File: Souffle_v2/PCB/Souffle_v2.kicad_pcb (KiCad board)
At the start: 2 copper layers, 137.2 x 109.2 mm, 81 parts, among them J1 LED, J2 4PIN, J3 OLED, SW1 SW_PUSH, SW10 SW_PUSH, SW11 SW_PUSH, SW12 SW_PUSH, SW13 SW_PUSH, SW14 SW_PUSH, SW15 SW_PUSH, SW16 SW_PUSH, SW17 SW_PUSH, SW18 SW_PUSH, SW19 SW_PUSH, SW2 SW_PUSH, SW20 SW_PUSH, SW21 SW_PUSH, SW22 SW_PUSH, SW23 SW_PUSH, SW24 SW_PUSH, SW25 SW_PUSH, SW25b1 RotaryEncoder_Switch, SW26 SW_PUSH, SW27 SW_PUSH, SW28 SW_PUSH, SW29 SW_PUSH, SW3 SW_PUSH, SW30 SW_PUSH, SW4 SW_PUSH, SW5 SW_PUSH, SW6 SW_PUSH, SW7 SW_PUSH, SW8 SW_PUSH, SW9 SW_PUSH, U1 ProMicro

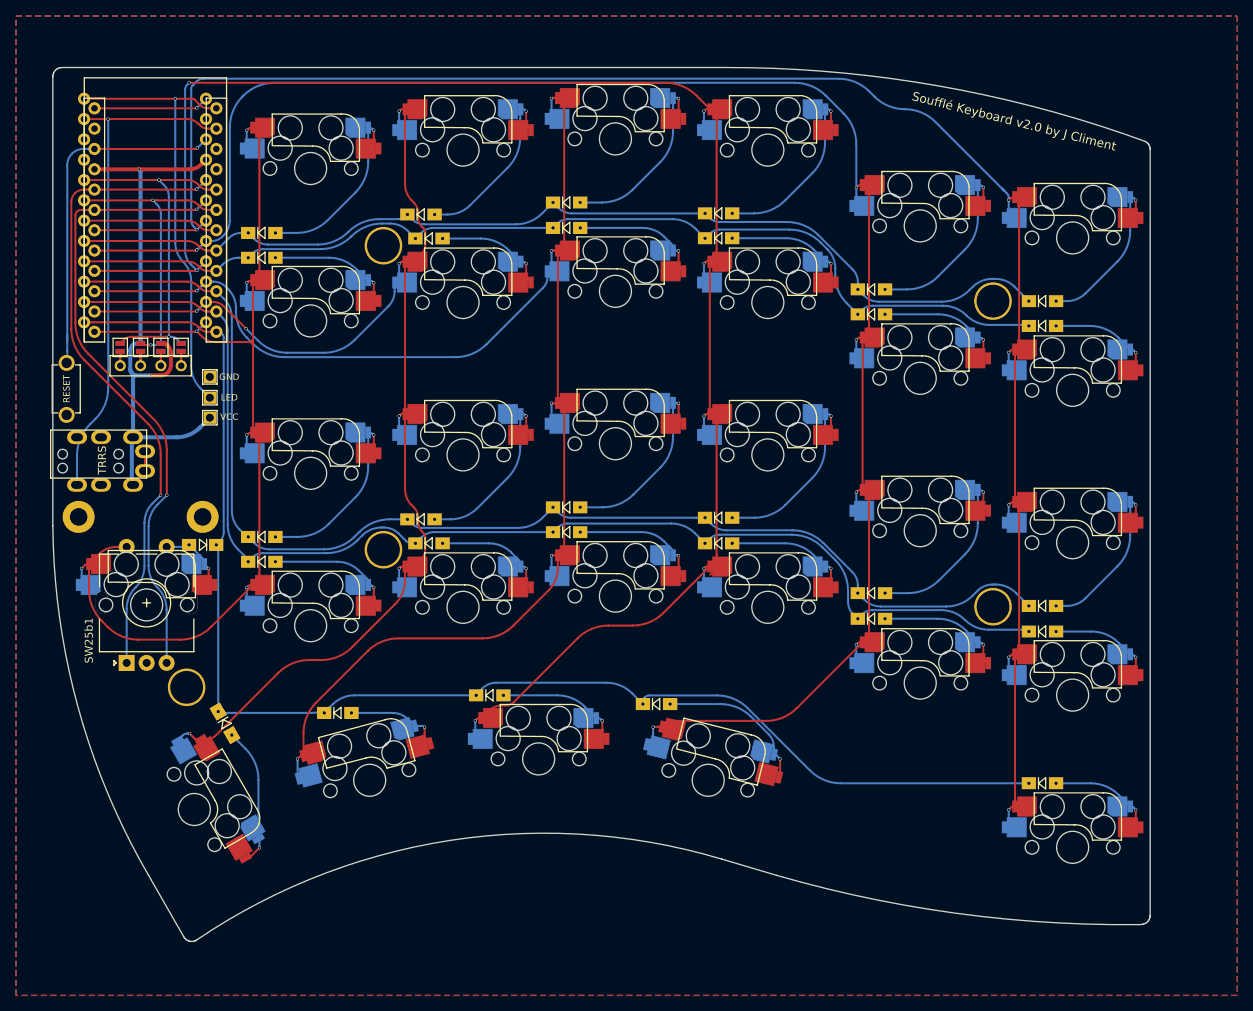
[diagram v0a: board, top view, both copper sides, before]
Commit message: Small fix for 2u keys in the thumb cluster touching the OLED key.
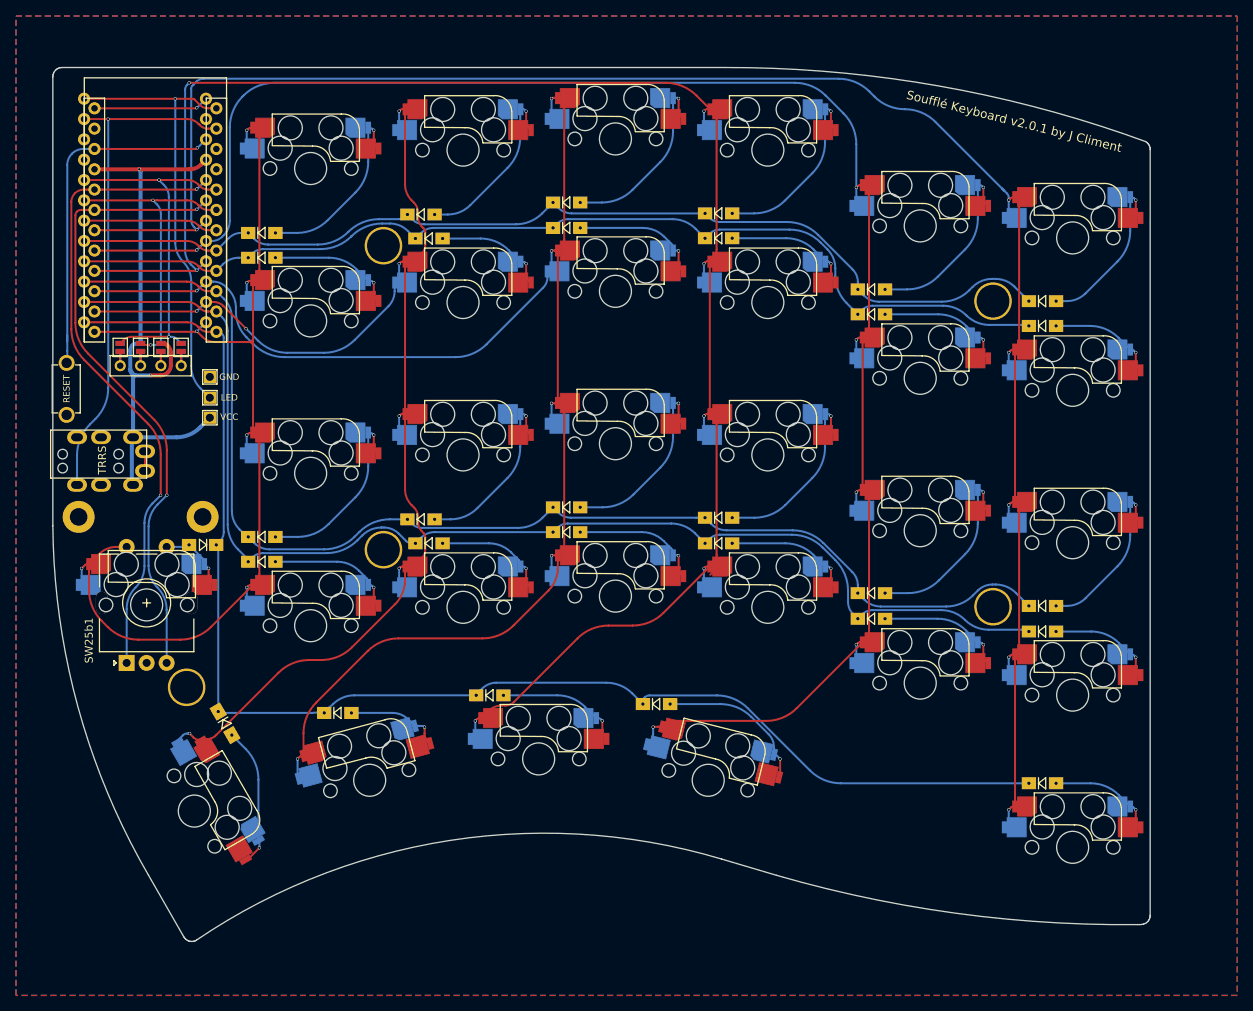
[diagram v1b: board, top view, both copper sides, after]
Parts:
- moved SW26 0.20 mm to (91.6, 125.7)
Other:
- board text added: "Soufflé Keyboard v2.0.1 by J Climent"
- board text removed: "Soufflé Keyboard v2.0 by J Climent"
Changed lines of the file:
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@@
   (setup
     (pad_to_mask_clearance 0)
-    (grid_origin 125.184 43.123139)
+    (grid_origin 91.594 125.543139)
     (pcbplotparams
       (layerselection 0x00010fc_ffffffff)
@@
       (drillshape 0)
       (scaleselection 1)
-      (outputdirectory "../../Gerbers/Souffle_v2/gerber/")
+      (outputdirectory "../../Gerbers/Souffle_v2/gerber2.0.1/")
     )
   )
@@
   )
   (footprint "SofleKeyboard-footprint:CherryMX_Hotswap_1.5_mod" (layer "F.Cu")
-    (at 91.594 125.543139 -60)
+    (at 91.594 125.743139 -60)
     (property "Sheetfile" "Souffle_v2.kicad_sch")
     (property "Sheetname" "")
@@
   (gr_arc (start 209.535 139.935639) (mid 186.721075 138.503894) (end 164.358 133.769139) (layer "Edge.Cuts") (width 0.1))
   (gr_line (start 90.552207 141.785459) (end 90.40507 141.641469) (layer "Edge.Cuts") (width 0.1))
-  (gr_text "Soufflé Keyboard v2.0 by J Climent" (at 194.076 39.535139 -14) (layer "B.SilkS")
+  (gr_text "Soufflé Keyboard v2.0.1 by J Climent" (at 194.076 39.535139 -14) (layer "B.SilkS")
     (effects (font (size 1.1 1.1) (thickness 0.2)) (justify mirror))
   )
-  (gr_text "Soufflé Keyboard v2.0 by J Climent\n" (at 194.076 39.535139 -14) (layer "F.SilkS")
+  (gr_text "Soufflé Keyboard v2.0.1 by J Climent\n" (at 194.076 39.535139 -14) (layer "F.SilkS")
     (effects (font (size 1.1 1.1) (thickness 0.2)))
   )
